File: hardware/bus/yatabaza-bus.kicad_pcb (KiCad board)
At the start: 2 copper layers, 94 x 65.4 mm, 26 parts, among them P1 POWER, P11 BUS, P12 BUS, P15 Φ, P16 Φ, P17 BUS, P18 POWER, P19 AUDIO, P2 POWER, P20 SUPPORT, P21 SUPPORT, P22 BUS, P23 POWER, P24 AUDIO, P25 SCREW, P26 SCREW, P27 SCREW, P28 SCREW, P29 SCREW, P3 L, P30 SCREW, P4 R, P6 HV, P7 HV, P8 L, P9 R

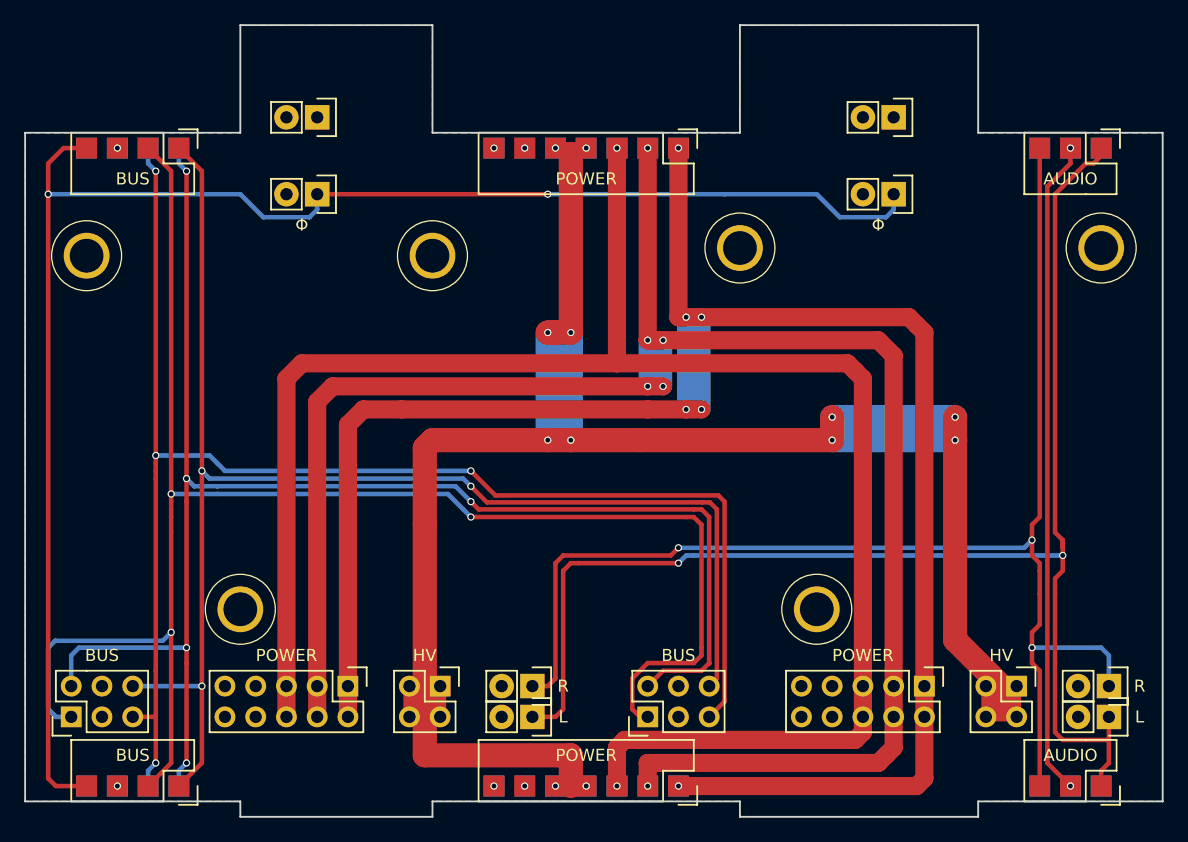
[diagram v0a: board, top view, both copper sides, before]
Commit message: ~ Ported hardware to Kicad6
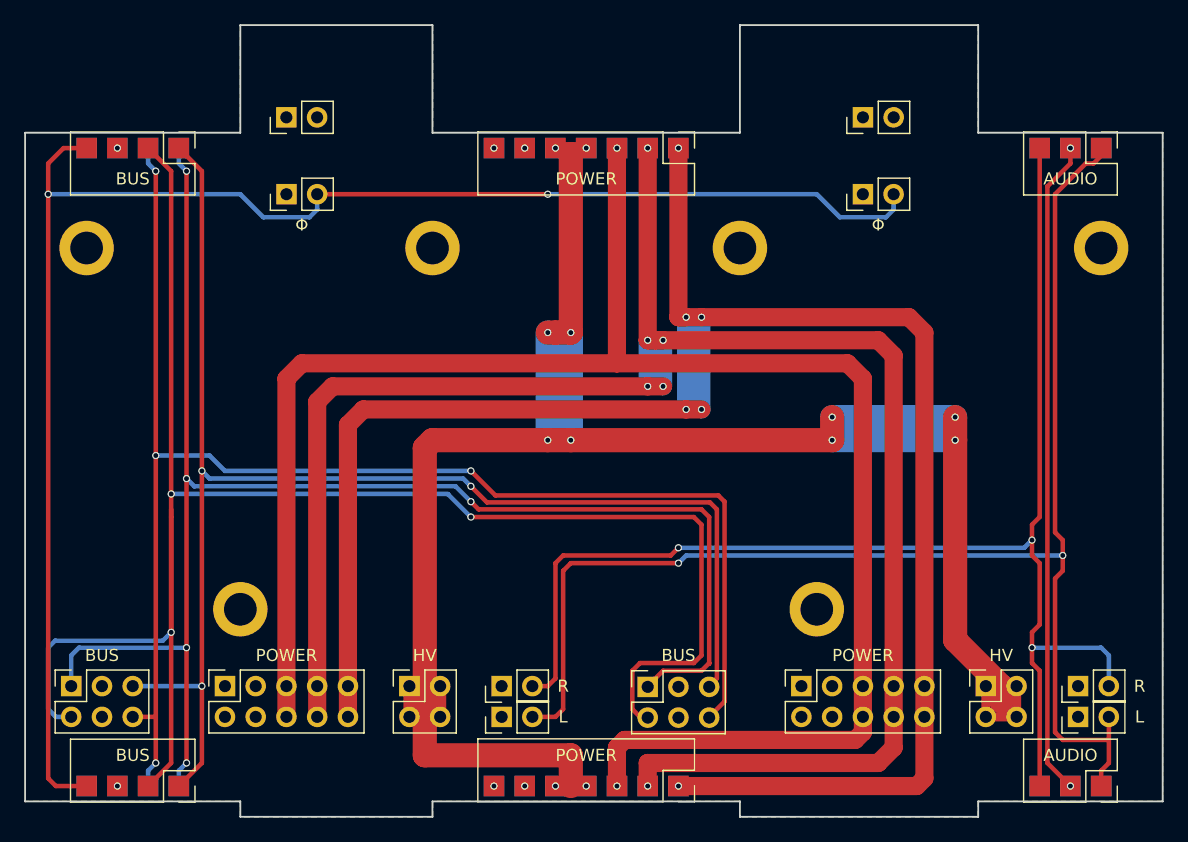
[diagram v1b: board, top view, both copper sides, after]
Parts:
- P1, P2: footprint Pin_Headers:Pin_Header_Straight_2x05 -> Connector_PinHeader_2.54mm:PinHeader_2x05_P2.54mm_Vertical
- P11, P12, P19, P24: footprint Pin_Headers:Pin_Header_Straight_2x03 -> Connector_PinHeader_2.54mm:PinHeader_2x03_P2.54mm_Vertical
- P15, P16, P20, P21, P3, P4, P8, P9: footprint Pin_Headers:Pin_Header_Straight_1x02 -> Connector_PinHeader_2.54mm:PinHeader_1x02_P2.54mm_Vertical
- P17, P22: footprint Pin_Headers:Pin_Header_Straight_2x04 -> Connector_PinHeader_2.54mm:PinHeader_2x04_P2.54mm_Vertical
- P18, P23: footprint Pin_Headers:Pin_Header_Straight_2x07 -> Connector_PinHeader_2.54mm:PinHeader_2x07_P2.54mm_Vertical
- P25, P26, P27, P28, P29, P30: footprint digikey-footprints:Test-Point-Pin_Drill2.79mm -> MountingHole:MountingHole_2.7mm_M2.5_ISO14580_Pad
- P6, P7: footprint Pin_Headers:Pin_Header_Straight_2x02 -> Connector_PinHeader_2.54mm:PinHeader_2x02_P2.54mm_Vertical
- moved P1 10.2 mm to (49.5, 78.7), turned to 90 degrees
- moved P2 10.2 mm to (97.2, 78.7), turned to 90 degrees
- moved P16 2.55 mm to (102.2, 38.1), turned to 90 degrees
- moved P20 2.55 mm to (54.6, 31.8), turned to 90 degrees
- moved P4 2.55 mm to (72.4, 78.7), turned to 90 degrees
- moved P7 2.55 mm to (112.4, 78.7), turned to 90 degrees
- moved P8 2.55 mm to (120.0, 81.3), turned to 90 degrees
- moved P9 2.55 mm to (120.0, 78.7), turned to 90 degrees
- moved P11 2.54 mm to (36.8, 78.7)
- moved P12 2.54 mm to (84.5, 78.7)
- moved P21 2.54 mm to (102.2, 31.8), turned to 90 degrees
- moved P22 2.54 mm to (45.7, 84.5)
- moved P23 2.54 mm to (87.0, 84.5)
- moved P24 2.54 mm to (121.9, 84.5)
- moved P3 2.54 mm to (72.4, 81.3), turned to 90 degrees
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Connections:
- P1 pad 1: +9VA -> GND
- P1 pad 10: GND -> +9VA
- P1 pad 2: +9VA -> GND
- P1 pad 3: -9VA -> GND
- P1 pad 4: -9VA -> GND
- P1 pad 7: GND -> -9VA
- P1 pad 8: GND -> -9VA
- P1 pad 9: GND -> +9VA
- P11 pad 1: /~RST -> /SCL
- P11 pad 2: /SCL -> /~{RST}
- P11 pad 5: /~IRQ -> /SDA
- P11 pad 6: /SDA -> /~{IRQ}
- P12 pad 1: /~RST -> /SCL
- P12 pad 2: /SCL -> /~{RST}
- P12 pad 5: /~IRQ -> /SDA
- P12 pad 6: /SDA -> /~{IRQ}
- P15 pad 1: /Φ_SYNTH -> GND
- P15 pad 2: GND -> /Φ_SYNTH
- P16 pad 1: /Φ_SYNTH -> GND
- P16 pad 2: GND -> /Φ_SYNTH
- P17 pad 3: /~RST -> /~{RST}
- P17 pad 4: /~IRQ -> /~{IRQ}
- P2 pad 1: +9VA -> GND
- P2 pad 10: GND -> +9VA
- P2 pad 2: +9VA -> GND
- P2 pad 3: -9VA -> GND
- P2 pad 4: -9VA -> GND
- P2 pad 7: GND -> -9VA
- P2 pad 8: GND -> -9VA
- P2 pad 9: GND -> +9VA
- P20 pad 1: Net-(P20-Pad1) -> unconnected-(P20-Pad1)
- P20 pad 2: Net-(P20-Pad2) -> unconnected-(P20-Pad2)
- P21 pad 1: Net-(P21-Pad1) -> unconnected-(P21-Pad1)
- P21 pad 2: Net-(P21-Pad2) -> unconnected-(P21-Pad2)
- P22 pad 3: /~RST -> /~{RST}
- P22 pad 4: /~IRQ -> /~{IRQ}
- P25 pad 1: Net-(P25-Pad1) -> unconnected-(P25-Pad1)
- P26 pad 1: Net-(P26-Pad1) -> unconnected-(P26-Pad1)
- P27 pad 1: Net-(P27-Pad1) -> unconnected-(P27-Pad1)
- P28 pad 1: Net-(P28-Pad1) -> unconnected-(P28-Pad1)
- P29 pad 1: Net-(P29-Pad1) -> unconnected-(P29-Pad1)
- P3 pad 1: /AUDIO_L -> GND
- P3 pad 2: GND -> /AUDIO_L
- P30 pad 1: Net-(P30-Pad1) -> unconnected-(P30-Pad1)
- P4 pad 1: /AUDIO_R -> GND
- P4 pad 2: GND -> /AUDIO_R
- P8 pad 1: /AUDIO_L -> GND
- P8 pad 2: GND -> /AUDIO_L
- P9 pad 1: /AUDIO_R -> GND
- P9 pad 2: GND -> /AUDIO_R
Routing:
- net /~{RST}: track 0.00 -> 149.0 mm, vias 0 -> 3
- net /~RST: track 140.0 -> 0.00 mm, vias 3 -> 0
- net /~{IRQ}: track 0.00 -> 122.0 mm, vias 0 -> 4
- net /~IRQ: track 122.0 -> 0.00 mm, vias 4 -> 0
- net -9VA: track 157.2 -> 155.9 mm
- net /SCL: track 129.4 -> 128.1 mm
- net +12V: track 189.4 -> 188.7 mm
- net /AUDIO_L: track 118.1 -> 117.5 mm
- net +9VA: track 162.6 -> 162.0 mm
- net +5V: track 148.3 -> 147.6 mm
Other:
- net class Default removed
- rule pad_to_mask_clearance: 0.2 -> 0
